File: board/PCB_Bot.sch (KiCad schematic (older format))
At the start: 16 parts, among them U1 TB6612FNG, U2 LSM9DS1

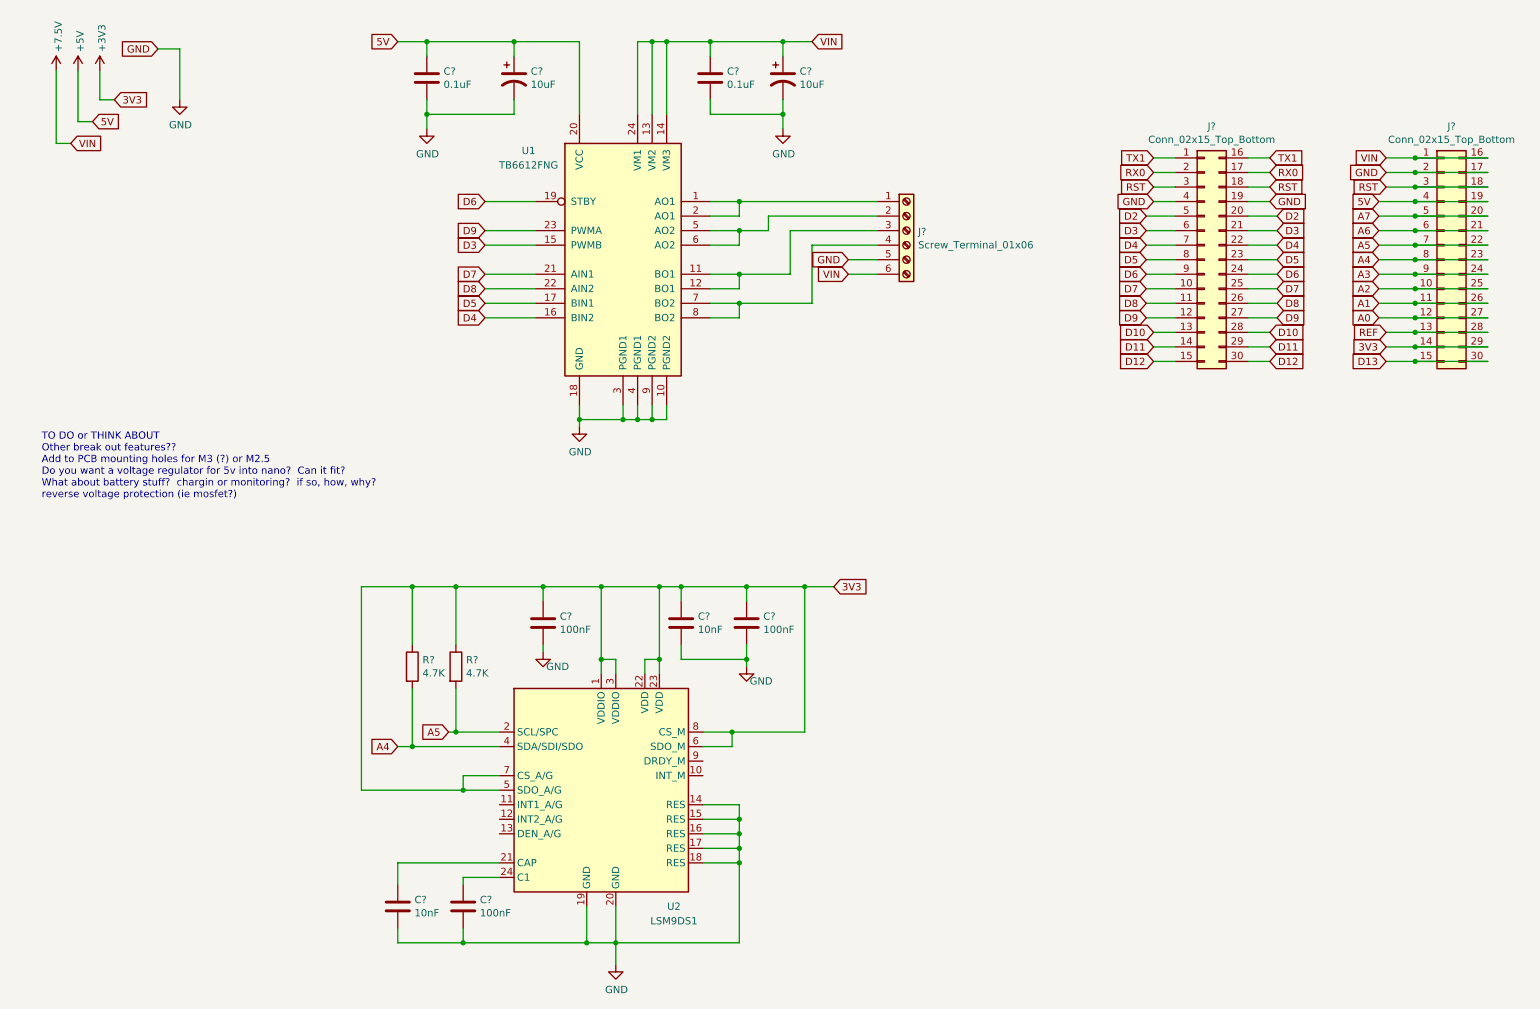
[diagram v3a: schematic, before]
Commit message: update pcbnew board layout and update foot prints
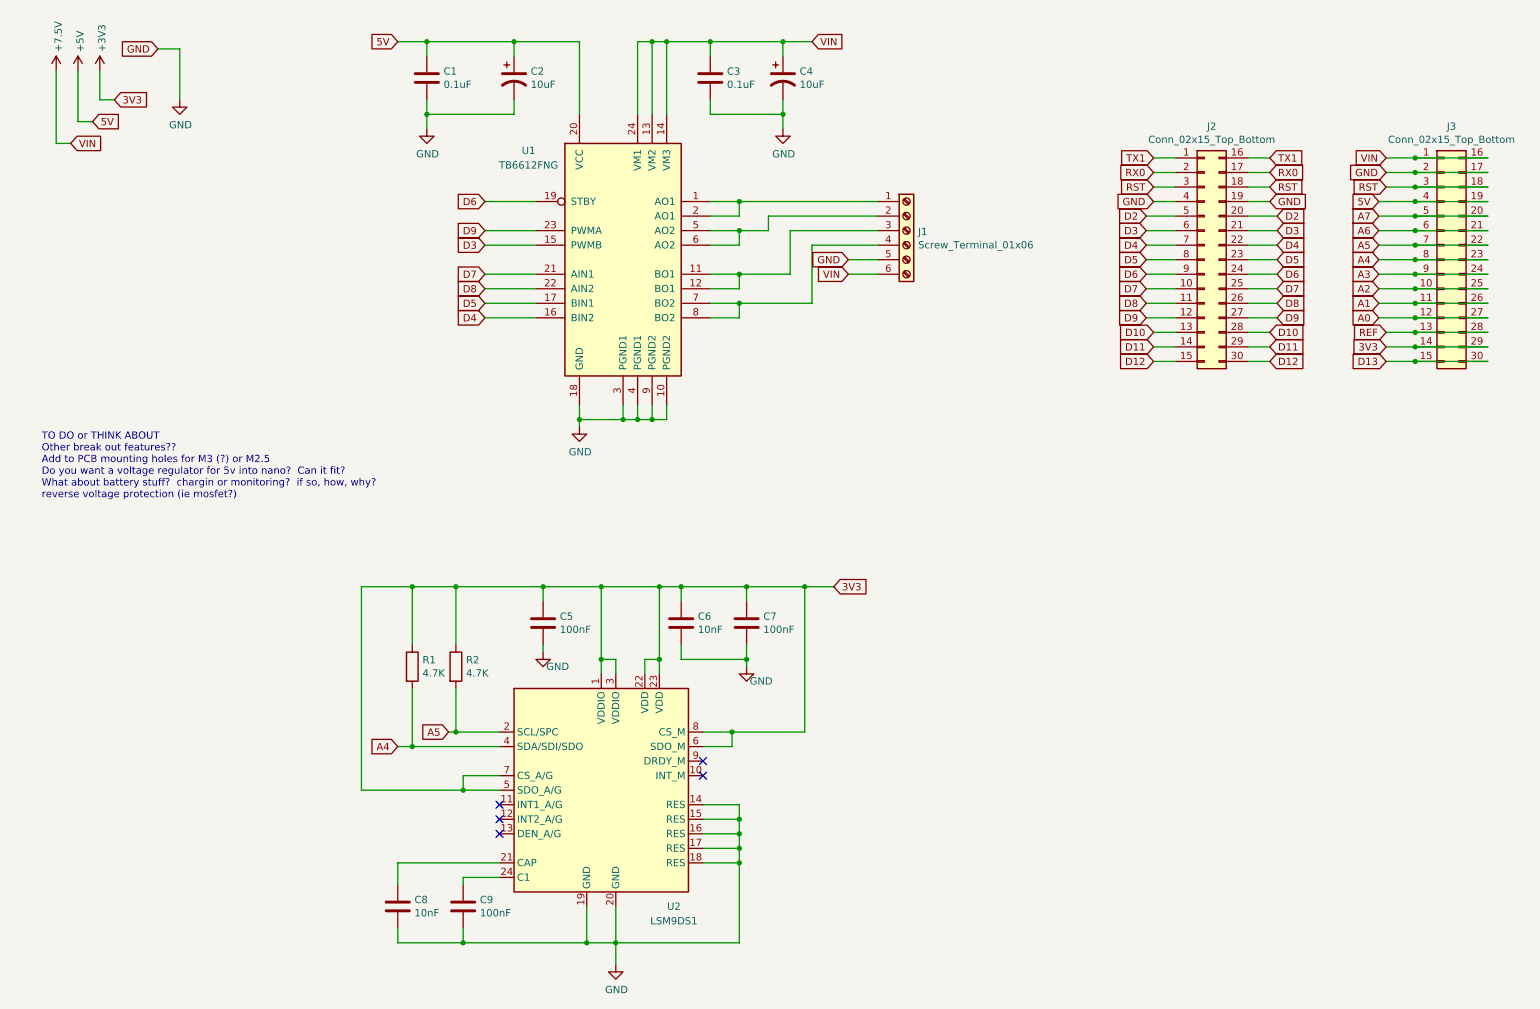
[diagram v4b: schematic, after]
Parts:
- C1, C3, C6, C8: renamed from C?; footprint (none) -> Capacitor_SMD:C_0603_1608Metric
- C2, C4, C5, C7, C9: renamed from C?; footprint (none) -> Capacitor_SMD:C_0805_2012Metric
- J1: renamed from J?; footprint (none) -> TerminalBlock_Phoenix:TerminalBlock_Phoenix_PTSM-0,5-5-2.5-V-THR_1x05_P2.50mm_Vertical
- J2: renamed from J?; footprint (none) -> Connector_PinSocket_2.54mm:PinSocket_2x15_P2.54mm_Vertical
- J3: renamed from J?; footprint (none) -> Connector_PinSocket_2.54mm:PinSocket_2x16_P2.54mm_Vertical
- R1, R2: renamed from R?; footprint (none) -> Resistor_SMD:R_0603_1608Metric
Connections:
- no-connect marks 0 -> 5
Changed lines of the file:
@@
 $EndComp
 $Comp
-L Connector_Generic:Conn_02x15_Top_Bottom J?
+L Connector_Generic:Conn_02x15_Top_Bottom J2
 U 1 1 5E50BAC2
 P 8650 2250
-F 0 "J?" H 8700 3167 50  0000 C CNN
+F 0 "J2" H 8700 3167 50  0000 C CNN
 F 1 "Conn_02x15_Top_Bottom" H 8700 3076 50  0000 C CNN
-F 2 "" H 8650 2250 50  0001 C CNN
+F 2 "Connector_PinSocket_2.54mm:PinSocket_2x15_P2.54mm_Vertical" H 8650 2250 50  0001 C CNN
 F 3 "~" H 8650 2250 50  0001 C CNN
 	1    8650 2250
@@
 $EndComp
 $Comp
-L Connector_Generic:Conn_02x15_Top_Bottom J?
+L Connector_Generic:Conn_02x15_Top_Bottom J3
 U 1 1 5E512BAE
 P 10300 2250
-F 0 "J?" H 10350 3167 50  0000 C CNN
+F 0 "J3" H 10350 3167 50  0000 C CNN
 F 1 "Conn_02x15_Top_Bottom" H 10350 3076 50  0000 C CNN
-F 2 "" H 10300 2250 50  0001 C CNN
+F 2 "Connector_PinSocket_2.54mm:PinSocket_2x16_P2.54mm_Vertical" H 10300 2250 50  0001 C CNN
 F 3 "~" H 10300 2250 50  0001 C CNN
 	1    10300 2250
@@
 Connection ~ 10100 2950
 $Comp
-L power:+3V3 #PWR?
+L power:+3V3 #PWR03
 U 1 1 5E559F29
 P 1050 950
-F 0 "#PWR?" H 1050 800 50  0001 C CNN
+F 0 "#PWR03" H 1050 800 50  0001 C CNN
 F 1 "+3V3" V 1065 1078 50  0000 L CNN
 F 2 "" H 1050 950 50  0001 C CNN
@@
 $EndComp
 $Comp
-L power:+5V #PWR?
+L power:+5V #PWR02
 U 1 1 5E55AD93
 P 900 950
-F 0 "#PWR?" H 900 800 50  0001 C CNN
+F 0 "#PWR02" H 900 800 50  0001 C CNN
 F 1 "+5V" V 915 1078 50  0000 L CNN
 F 2 "" H 900 950 50  0001 C CNN
@@
 TO DO or THINK ABOUT\nOther break out features??\nAdd to PCB mounting holes for M3 (?) or M2.5\nDo you want a voltage regulator for 5v into nano?  Can it fit?\nWhat about battery stuff?  chargin or monitoring?  if so, how, why?\nreverse voltage protection (ie mosfet?)
 $Comp
-L power:+7.5V #PWR?
+L power:+7.5V #PWR01
 U 1 1 5E560050
 P 750 950
-F 0 "#PWR?" H 750 800 50  0001 C CNN
+F 0 "#PWR01" H 750 800 50  0001 C CNN
 F 1 "+7.5V" V 765 1078 50  0000 L CNN
 F 2 "" H 750 950 50  0001 C CNN
@@
 	3700 2550 4050 2550
 $Comp
-L power:GND #PWR?
+L power:GND #PWR07
 U 1 1 5E535007
 P 4350 3400
-F 0 "#PWR?" H 4350 3150 50  0001 C CNN
+F 0 "#PWR07" H 4350 3150 50  0001 C CNN
 F 1 "GND" H 4355 3227 50  0000 C CNN
 F 2 "" H 4350 3400 50  0001 C CNN
@@
 	3700 2350 4050 2350
 $Comp
-L Device:C C?
+L Device:C C3
 U 1 1 5E546099
 P 5250 1000
-F 0 "C?" H 5365 1046 50  0000 L CNN
+F 0 "C3" H 5365 1046 50  0000 L CNN
 F 1 "0.1uF" H 5365 955 50  0000 L CNN
-F 2 "" H 5288 850 50  0001 C CNN
+F 2 "Capacitor_SMD:C_0603_1608Metric" H 5288 850 50  0001 C CNN
 F 3 "~" H 5250 1000 50  0001 C CNN
 	1    5250 1000
@@
 $EndComp
 $Comp
-L Device:C C?
+L Device:C C1
 U 1 1 5E58DEAB
 P 3300 1000
-F 0 "C?" H 3415 1046 50  0000 L CNN
+F 0 "C1" H 3415 1046 50  0000 L CNN
 F 1 "0.1uF" H 3415 955 50  0000 L CNN
-F 2 "" H 3338 850 50  0001 C CNN
+F 2 "Capacitor_SMD:C_0603_1608Metric" H 3338 850 50  0001 C CNN
 F 3 "~" H 3300 1000 50  0001 C CNN
 	1    3300 1000
@@
 $EndComp
 $Comp
-L power:GND #PWR?
+L power:GND #PWR05
 U 1 1 5E591658
 P 3300 1350
-F 0 "#PWR?" H 3300 1100 50  0001 C CNN
+F 0 "#PWR05" H 3300 1100 50  0001 C CNN
 F 1 "GND" H 3305 1177 50  0000 C CNN
 F 2 "" H 3300 1350 50  0001 C CNN
@@
 $EndComp
 $Comp
-L power:GND #PWR?
+L power:GND #PWR06
 U 1 1 5E59215C
 P 5750 1350
-F 0 "#PWR?" H 5750 1100 50  0001 C CNN
+F 0 "#PWR06" H 5750 1100 50  0001 C CNN
 F 1 "GND" H 5755 1177 50  0000 C CNN
 F 2 "" H 5750 1350 50  0001 C CNN
@@
 	5750 1250 5750 1350
 $Comp
-L Device:CP1 C?
+L Device:CP1 C4
 U 1 1 5E5ACC00
 P 5750 1000
-F 0 "C?" H 5865 1046 50  0000 L CNN
+F 0 "C4" H 5865 1046 50  0000 L CNN
 F 1 "10uF" H 5865 955 50  0000 L CNN
-F 2 "" H 5750 1000 50  0001 C CNN
+F 2 "Capacitor_SMD:C_0805_2012Metric" H 5750 1000 50  0001 C CNN
 F 3 "~" H 5750 1000 50  0001 C CNN
 	1    5750 1000
@@
 $EndComp
 $Comp
-L Device:CP1 C?
+L Device:CP1 C2
 U 1 1 5E5ADB00
 P 3900 1000
-F 0 "C?" H 4015 1046 50  0000 L CNN
+F 0 "C2" H 4015 1046 50  0000 L CNN
 F 1 "10uF" H 4015 955 50  0000 L CNN
-F 2 "" H 3900 1000 50  0001 C CNN
+F 2 "Capacitor_SMD:C_0805_2012Metric" H 3900 1000 50  0001 C CNN
 F 3 "~" H 3900 1000 50  0001 C CNN
 	1    3900 1000
@@
 	1050 1150 1150 1150
 $Comp
-L power:GND #PWR?
+L power:GND #PWR04
 U 1 1 5E51BDF2
 P 1600 1150
-F 0 "#PWR?" H 1600 900 50  0001 C CNN
+F 0 "#PWR04" H 1600 900 50  0001 C CNN
 F 1 "GND" H 1605 977 50  0000 C CNN
 F 2 "" H 1600 1150 50  0001 C CNN
@@
 $EndComp
 $Comp
-L power:GND #PWR?
+L power:GND #PWR010
 U 1 1 5E6B0C8B
 P 4600 7100
-F 0 "#PWR?" H 4600 6850 50  0001 C CNN
+F 0 "#PWR010" H 4600 6850 50  0001 C CNN
 F 1 "GND" H 4605 6927 50  0000 C CNN
 F 2 "" H 4600 7100 50  0001 C CNN
@@
 	5450 6400 5450 6950
 $Comp
-L Device:C C?
+L Device:C C9
 U 1 1 5E6E7691
 P 3550 6700
-F 0 "C?" H 3665 6746 50  0000 L CNN
+F 0 "C9" H 3665 6746 50  0000 L CNN
 F 1 "100nF" H 3665 6655 50  0000 L CNN
-F 2 "" H 3588 6550 50  0001 C CNN
+F 2 "Capacitor_SMD:C_0805_2012Metric" H 3588 6550 50  0001 C CNN
 F 3 "~" H 3550 6700 50  0001 C CNN
 	1    3550 6700
@@
 $EndComp
 $Comp
-L Device:C C?
+L Device:C C8
 U 1 1 5E6E884E
 P 3100 6700
-F 0 "C?" H 3215 6746 50  0000 L CNN
+F 0 "C8" H 3215 6746 50  0000 L CNN
 F 1 "10nF" H 3215 6655 50  0000 L CNN
-F 2 "" H 3138 6550 50  0001 C CNN
+F 2 "Capacitor_SMD:C_0603_1608Metric" H 3138 6550 50  0001 C CNN
 F 3 "~" H 3100 6700 50  0001 C CNN
 	1    3100 6700
@@
 VIN
 $Comp
-L power:GND #PWR?
+L power:GND #PWR09
 U 1 1 5E769C6B
 P 5500 5050
-F 0 "#PWR?" H 5500 4800 50  0001 C CNN
+F 0 "#PWR09" H 5500 4800 50  0001 C CNN
 F 1 "GND" H 5600 4950 50  0000 C CNN
 F 2 "" H 5500 5050 50  0001 C CNN
@@
 $EndComp
 $Comp
-L power:GND #PWR?
+L power:GND #PWR08
 U 1 1 5E76A1FF
 P 4100 4950
-F 0 "#PWR?" H 4100 4700 50  0001 C CNN
+F 0 "#PWR08" H 4100 4700 50  0001 C CNN
 F 1 "GND" H 4200 4850 50  0000 C CNN
 F 2 "" H 4100 4950 50  0001 C CNN
@@
 $EndComp
 $Comp
-L Device:C C?
+L Device:C C6
 U 1 1 5E731103
 P 5050 4750
-F 0 "C?" H 5165 4796 50  0000 L CNN
+F 0 "C6" H 5165 4796 50  0000 L CNN
 F 1 "10nF" H 5165 4705 50  0000 L CNN
-F 2 "" H 5088 4600 50  0001 C CNN
+F 2 "Capacitor_SMD:C_0603_1608Metric" H 5088 4600 50  0001 C CNN
 F 3 "~" H 5050 4750 50  0001 C CNN
 	1    5050 4750
@@
 $EndComp
 $Comp
-L Device:C C?
+L Device:C C7
 U 1 1 5E732AB1
 P 5500 4750
-F 0 "C?" H 5615 4796 50  0000 L CNN
+F 0 "C7" H 5615 4796 50  0000 L CNN
 F 1 "100nF" H 5615 4705 50  0000 L CNN
-F 2 "" H 5538 4600 50  0001 C CNN
+F 2 "Capacitor_SMD:C_0805_2012Metric" H 5538 4600 50  0001 C CNN
 F 3 "~" H 5500 4750 50  0001 C CNN
 	1    5500 4750
@@
 $EndComp
 $Comp
-L Device:C C?
+L Device:C C5
 U 1 1 5E73342D
 P 4100 4750
-F 0 "C?" H 4215 4796 50  0000 L CNN
+F 0 "C5" H 4215 4796 50  0000 L CNN
 F 1 "100nF" H 4215 4705 50  0000 L CNN
-F 2 "" H 4138 4600 50  0001 C CNN
+F 2 "Capacitor_SMD:C_0805_2012Metric" H 4138 4600 50  0001 C CNN
 F 3 "~" H 4100 4750 50  0001 C CNN
 	1    4100 4750
@@
 	5200 5500 5400 5500
 $Comp
-L Device:R R?
+L Device:R R2
 U 1 1 5E8B4EDF
 P 3500 5050
-F 0 "R?" H 3570 5096 50  0000 L CNN
+F 0 "R2" H 3570 5096 50  0000 L CNN
 F 1 "4.7K" H 3570 5005 50  0000 L CNN
-F 2 "" V 3430 5050 50  0001 C CNN
+F 2 "Resistor_SMD:R_0603_1608Metric" V 3430 5050 50  0001 C CNN
 F 3 "~" H 3500 5050 50  0001 C CNN
 	1    3500 5050
@@
 $EndComp
 $Comp
-L Device:R R?
+L Device:R R1
 U 1 1 5E8B57A0
 P 3200 5050
-F 0 "R?" H 3270 5096 50  0000 L CNN
+F 0 "R1" H 3270 5096 50  0000 L CNN
 F 1 "4.7K" H 3270 5005 50  0000 L CNN
-F 2 "" V 3130 5050 50  0001 C CNN
+F 2 "Resistor_SMD:R_0603_1608Metric" V 3130 5050 50  0001 C CNN
 F 3 "~" H 3200 5050 50  0001 C CNN
 	1    3200 5050
@@
 $EndBitmap
 $Comp
-L Connector:Screw_Terminal_01x06 J?
+L Connector:Screw_Terminal_01x06 J1
 U 1 1 5EAC1545
 P 6600 2050
-F 0 "J?" H 6680 2042 50  0000 L CNN
+F 0 "J1" H 6680 2042 50  0000 L CNN
 F 1 "Screw_Terminal_01x06" H 6680 1951 50  0000 L CNN
-F 2 "" H 6600 2050 50  0001 C CNN
+F 2 "TerminalBlock_Phoenix:TerminalBlock_Phoenix_PTSM-0,5-5-2.5-V-THR_1x05_P2.50mm_Vertical" H 6600 2050 50  0001 C CNN
 F 3 "~" H 6600 2050 50  0001 C CNN
 	1    6600 2050
@@
 Wire Wire Line
 	6200 2350 6400 2350
+NoConn ~ 5200 5700
+NoConn ~ 5200 5800
+NoConn ~ 3800 6000
+NoConn ~ 3800 6100
+NoConn ~ 3800 6200
 $EndSCHEMATC

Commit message: Change connectors in schematic and in pcbnew.  add some tracks in pcbnew
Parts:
- J2: symbol Connector_Generic:Conn_02x15_Top_Bottom -> Connector_Generic:Conn_02x15_Odd_Even
- J3: footprint Connector_PinSocket_2.54mm:PinSocket_2x16_P2.54mm_Vertical -> Connector_PinSocket_2.54mm:PinSocket_2x15_P2.54mm_Vertical; symbol Connector_Generic:Conn_02x15_Top_Bottom -> Connector_Generic:Conn_02x15_Odd_Even
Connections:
- net +3V3: now also J3.27 (Pin_27), J3.28 (Pin_28); no longer J3.14 (Pin_14), J3.29 (Pin_29)
- net +5V: now also J3.7 (Pin_7), J3.8 (Pin_8); no longer J3.19 (Pin_19), J3.4 (Pin_4)
- net +7.5V: now also J3.2 (Pin_2); no longer J3.16 (Pin_16)
- net A0: now also J3.23 (Pin_23), J3.24 (Pin_24); no longer J3.12 (Pin_12), J3.27 (Pin_27)
- net A1: now also J3.21 (Pin_21), J3.22 (Pin_22); no longer J3.11 (Pin_11), J3.26 (Pin_26)
- net A2: now also J3.19 (Pin_19), J3.20 (Pin_20); no longer J3.10 (Pin_10), J3.25 (Pin_25)
- net A3: now also J3.17 (Pin_17), J3.18 (Pin_18); no longer J3.24 (Pin_24), J3.9 (Pin_9)
- net A4: now also J3.15 (Pin_15), J3.16 (Pin_16); no longer J3.23 (Pin_23), J3.8 (Pin_8)
- net A5: now also J3.13 (Pin_13), J3.14 (Pin_14); no longer J3.22 (Pin_22), J3.7 (Pin_7)
- net A6: now also J3.11 (Pin_11), J3.12 (Pin_12); no longer J3.21 (Pin_21), J3.6 (Pin_6)
- net A7: now also J3.10 (Pin_10), J3.9 (Pin_9); no longer J3.20 (Pin_20), J3.5 (Pin_5)
- net D10: now also J2.25 (Pin_25), J2.26 (Pin_26); no longer J2.13 (Pin_13), J2.28 (Pin_28)
- net D11: now also J2.27 (Pin_27), J2.28 (Pin_28); no longer J2.14 (Pin_14), J2.29 (Pin_29)
- net D12: now also J2.29 (Pin_29); no longer J2.15 (Pin_15)
- net D13: now also J3.29 (Pin_29); no longer J3.15 (Pin_15)
- net D2: now also J2.10 (Pin_10), J2.9 (Pin_9); no longer J2.20 (Pin_20), J2.5 (Pin_5)
- net D3: now also J2.11 (Pin_11), J2.12 (Pin_12); no longer J2.21 (Pin_21), J2.6 (Pin_6)
- net D4: now also J2.13 (Pin_13), J2.14 (Pin_14); no longer J2.22 (Pin_22), J2.7 (Pin_7)
- net D5: now also J2.15 (Pin_15), J2.16 (Pin_16); no longer J2.23 (Pin_23), J2.8 (Pin_8)
- net D6: now also J2.17 (Pin_17), J2.18 (Pin_18); no longer J2.24 (Pin_24), J2.9 (Pin_9)
- net D7: now also J2.19 (Pin_19), J2.20 (Pin_20); no longer J2.10 (Pin_10), J2.25 (Pin_25)
- net D8: now also J2.21 (Pin_21), J2.22 (Pin_22); no longer J2.11 (Pin_11), J2.26 (Pin_26)
- net D9: now also J2.23 (Pin_23), J2.24 (Pin_24); no longer J2.12 (Pin_12), J2.27 (Pin_27)
- net GND: now also J2.7 (Pin_7), J2.8 (Pin_8), J3.3 (Pin_3), J3.4 (Pin_4); no longer J2.19 (Pin_19), J2.4 (Pin_4), J3.17 (Pin_17), J3.2 (Pin_2)
- net REF: now also J3.25 (Pin_25), J3.26 (Pin_26); no longer J3.13 (Pin_13), J3.28 (Pin_28)
- net RST: now also J2.5 (Pin_5), J2.6 (Pin_6), J3.5 (Pin_5), J3.6 (Pin_6); no longer J2.18 (Pin_18), J2.3 (Pin_3), J3.18 (Pin_18), J3.3 (Pin_3)
- net RX0: now also J2.3 (Pin_3), J2.4 (Pin_4); no longer J2.17 (Pin_17), J2.2 (Pin_2)
- net TX1: now also J2.2 (Pin_2); no longer J2.16 (Pin_16)
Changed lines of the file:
@@
 $EndComp
 $Comp
-L Connector_Generic:Conn_02x15_Top_Bottom J2
+L Connector_Generic:Conn_02x15_Odd_Even J2
 U 1 1 5E50BAC2
 P 8650 2250
@@
 	1    0    0    -1
 $EndComp
-$Comp
-L Connector_Generic:Conn_02x15_Top_Bottom J3
-U 1 1 5E512BAE
-P 10300 2250
-F 0 "J3" H 10350 3167 50  0000 C CNN
-F 1 "Conn_02x15_Top_Bottom" H 10350 3076 50  0000 C CNN
-F 2 "Connector_PinSocket_2.54mm:PinSocket_2x16_P2.54mm_Vertical" H 10300 2250 50  0001 C CNN
-F 3 "~" H 10300 2250 50  0001 C CNN
-	1    10300 2250
-	1    0    0    -1
-$EndComp
 Text GLabel 9100 1550 2    50   Input ~ 0
 TX1
@@
 Text GLabel 9900 2950 0    50   Input ~ 0
 D13
-Wire Wire Line
-	9900 1550 10100 1550
-Wire Wire Line
-	9900 1650 10100 1650
-Wire Wire Line
-	9900 1750 10100 1750
-Wire Wire Line
-	9850 1850 10100 1850
-Wire Wire Line
-	10100 1950 9850 1950
-Wire Wire Line
-	9850 2050 10100 2050
-Wire Wire Line
-	10100 2150 9850 2150
-Wire Wire Line
-	9850 2250 10100 2250
-Wire Wire Line
-	9850 2350 10100 2350
-Wire Wire Line
-	10100 2450 9850 2450
-Wire Wire Line
-	9850 2550 10100 2550
-Wire Wire Line
-	10100 2650 9850 2650
-Wire Wire Line
-	9900 2750 10100 2750
-Wire Wire Line
-	10100 2850 9900 2850
-Wire Wire Line
-	9900 2950 10100 2950
-Wire Wire Line
-	10600 1550 10100 1550
-Connection ~ 10100 1550
-Wire Wire Line
-	10100 1650 10600 1650
-Connection ~ 10100 1650
-Wire Wire Line
-	10100 1750 10600 1750
-Connection ~ 10100 1750
-Wire Wire Line
-	10100 1850 10600 1850
-Connection ~ 10100 1850
-Wire Wire Line
-	10100 1950 10600 1950
-Connection ~ 10100 1950
-Wire Wire Line
-	10100 2050 10600 2050
-Connection ~ 10100 2050
-Wire Wire Line
-	10100 2150 10600 2150
-Connection ~ 10100 2150
-Wire Wire Line
-	10600 2250 10100 2250
-Connection ~ 10100 2250
-Wire Wire Line
-	10100 2350 10600 2350
-Connection ~ 10100 2350
-Wire Wire Line
-	10100 2450 10600 2450
-Connection ~ 10100 2450
-Wire Wire Line
-	10100 2550 10600 2550
-Connection ~ 10100 2550
-Wire Wire Line
-	10100 2650 10600 2650
-Connection ~ 10100 2650
-Wire Wire Line
-	10100 2750 10600 2750
-Connection ~ 10100 2750
-Wire Wire Line
-	10100 2850 10600 2850
-Connection ~ 10100 2850
-Wire Wire Line
-	10100 2950 10600 2950
-Connection ~ 10100 2950
 $Comp
 L power:+3V3 #PWR03
@@
 NoConn ~ 3800 6100
 NoConn ~ 3800 6200
+Connection ~ 10100 2950
+Connection ~ 10100 2850
+Connection ~ 10100 2750
+Connection ~ 10100 2650
+Connection ~ 10100 2550
+Connection ~ 10100 2450
+Connection ~ 10100 2350
+Connection ~ 10100 2250
+Connection ~ 10100 2150
+Connection ~ 10100 2050
+Connection ~ 10100 1950
+Connection ~ 10100 1850
+Connection ~ 10100 1750
+Connection ~ 10100 1650
+Connection ~ 10100 1550
+Wire Wire Line
+	10100 2950 10600 2950
+Wire Wire Line
+	9900 2950 10100 2950
+Wire Wire Line
+	10100 2850 10600 2850
+Wire Wire Line
+	10100 2850 9900 2850
+Wire Wire Line
+	10100 2750 10600 2750
+Wire Wire Line
+	9900 2750 10100 2750
+Wire Wire Line
+	10100 2650 10600 2650
+Wire Wire Line
+	10100 2650 9850 2650
+Wire Wire Line
+	10100 2450 10600 2450
+Wire Wire Line
+	10100 2450 9850 2450
+Wire Wire Line
+	10100 2350 10600 2350
+Wire Wire Line
+	9850 2350 10100 2350
+Wire Wire Line
+	10600 2250 10100 2250
+Wire Wire Line
+	9850 2250 10100 2250
+Wire Wire Line
+	10100 2150 10600 2150
+Wire Wire Line
+	10100 2150 9850 2150
+Wire Wire Line
+	10100 1950 10600 1950
+Wire Wire Line
+	10100 1950 9850 1950
+Wire Wire Line
+	10100 1850 10600 1850
+Wire Wire Line
+	9850 1850 10100 1850
+Wire Wire Line
+	10100 1750 10600 1750
+Wire Wire Line
+	9900 1750 10100 1750
+Wire Wire Line
+	10100 1650 10600 1650
+Wire Wire Line
+	9900 1650 10100 1650
+Wire Wire Line
+	10600 1550 10100 1550
+Wire Wire Line
+	9900 1550 10100 1550
+Wire Wire Line
+	9850 2550 10100 2550
+Wire Wire Line
+	10100 2550 10600 2550
+Wire Wire Line
+	10100 2050 10600 2050
+Wire Wire Line
+	9850 2050 10100 2050
+$Comp
+L Connector_Generic:Conn_02x15_Odd_Even J3
+U 1 1 5E512BAE
+P 10300 2250
+F 0 "J3" H 10350 3167 50  0000 C CNN
+F 1 "Conn_02x15_Top_Bottom" H 10350 3076 50  0000 C CNN
+F 2 "Connector_PinSocket_2.54mm:PinSocket_2x15_P2.54mm_Vertical" H 10300 2250 50  0001 C CNN
+F 3 "~" H 10300 2250 50  0001 C CNN
+	1    10300 2250
+	1    0    0    -1
+$EndComp
 $EndSCHEMATC
